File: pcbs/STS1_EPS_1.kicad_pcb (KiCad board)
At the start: 4 copper layers, 81 x 85 mm, 104 parts, among them J2 Panel X+, J3 Battery Pack, J4 Panel X-, J5 Panel Y+, J6 Panel Y-, J7 Panel Z+, Q1 SI7135DP-T1-GE3, U1 LTC4020EUHFPBF, U10 MAX11632EEGT, U11 TMCS1101A3B-Q1, U12 BD50GA5WEFJ, U13 TMCS1101A3B-Q1, U14 LM334M, U15 LM334M, U16 LM334M, U17 LM334M, U18 LM334M, U19 TMCS1101A3B-Q1, U20 TMCS1101A3B-Q1, U21 TMCS1101A3B-Q1, U22 TMCS1101A3B-Q1, U23 TMCS1101A3B-Q1, U24 TMCS1101A3B-Q1, U25 TMCS1101A3B-Q1, U26 TMCS1101A3B-Q1, U4 BQ29209DRBT, U5 MAX11632EEGT, U6 MAX11632EEGT, U7 MAX11632EEGT, U8 MAX11632EEGT, U9 MAX11632EEGT

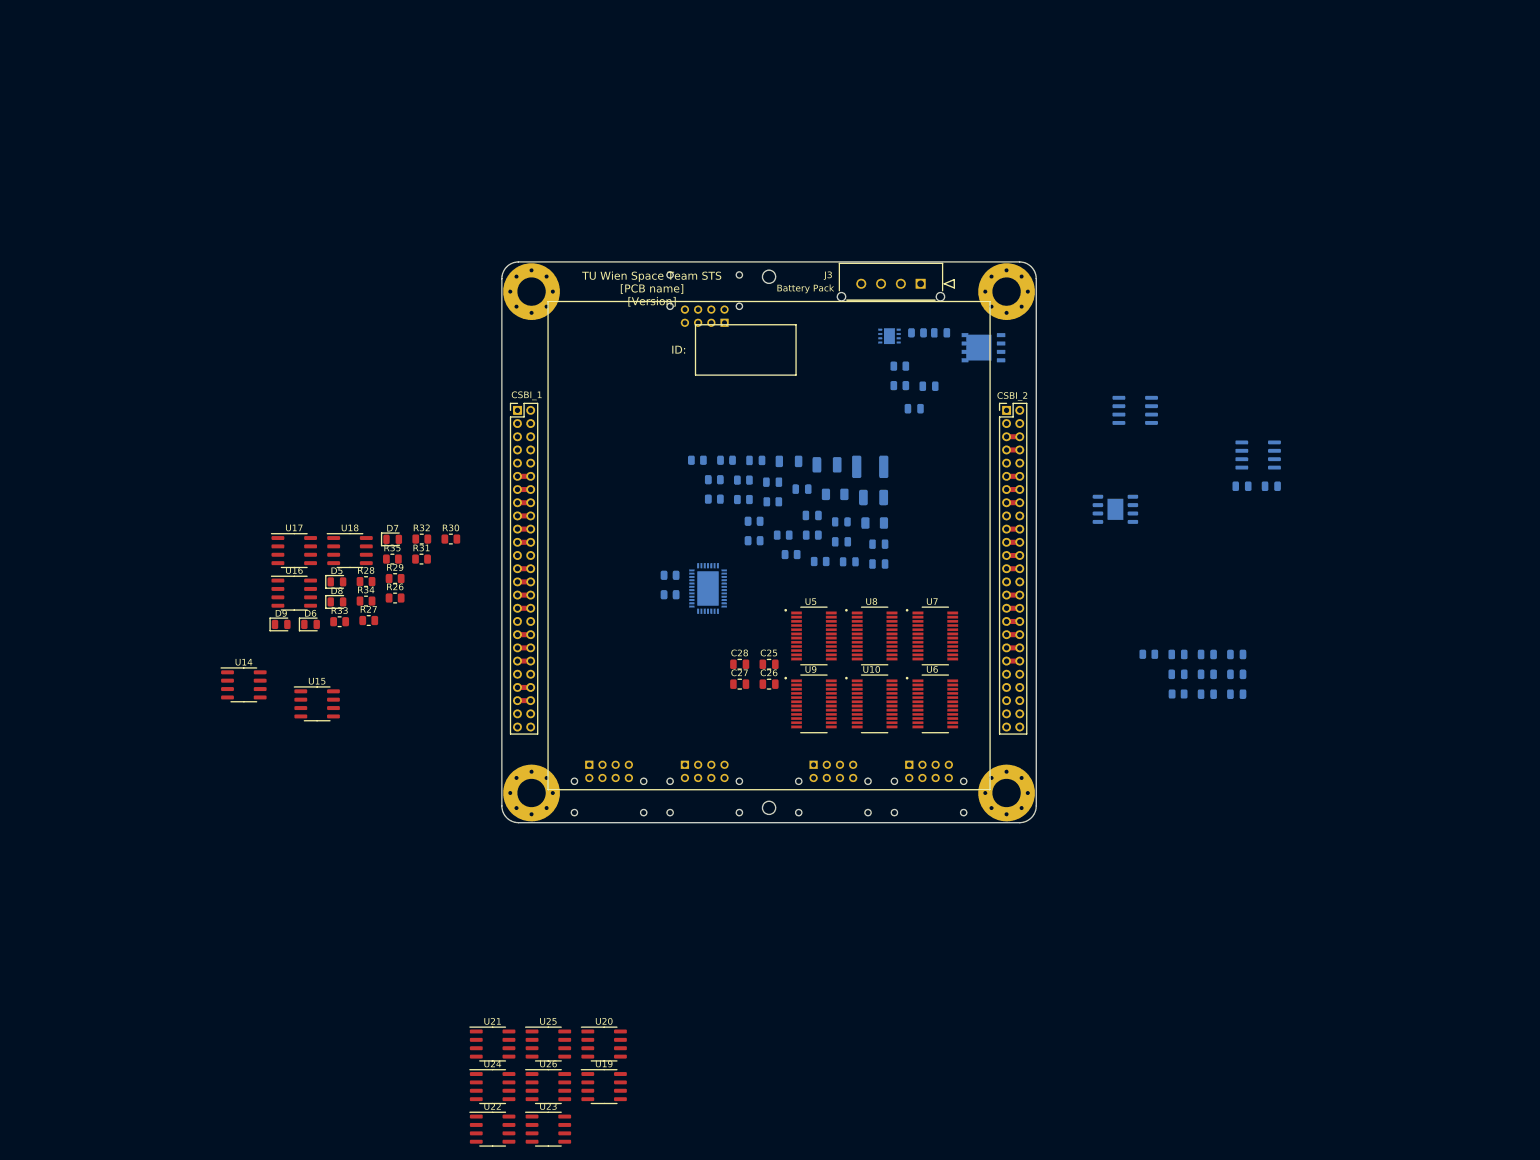
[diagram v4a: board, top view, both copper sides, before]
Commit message: Worked on STS_EPS_1.
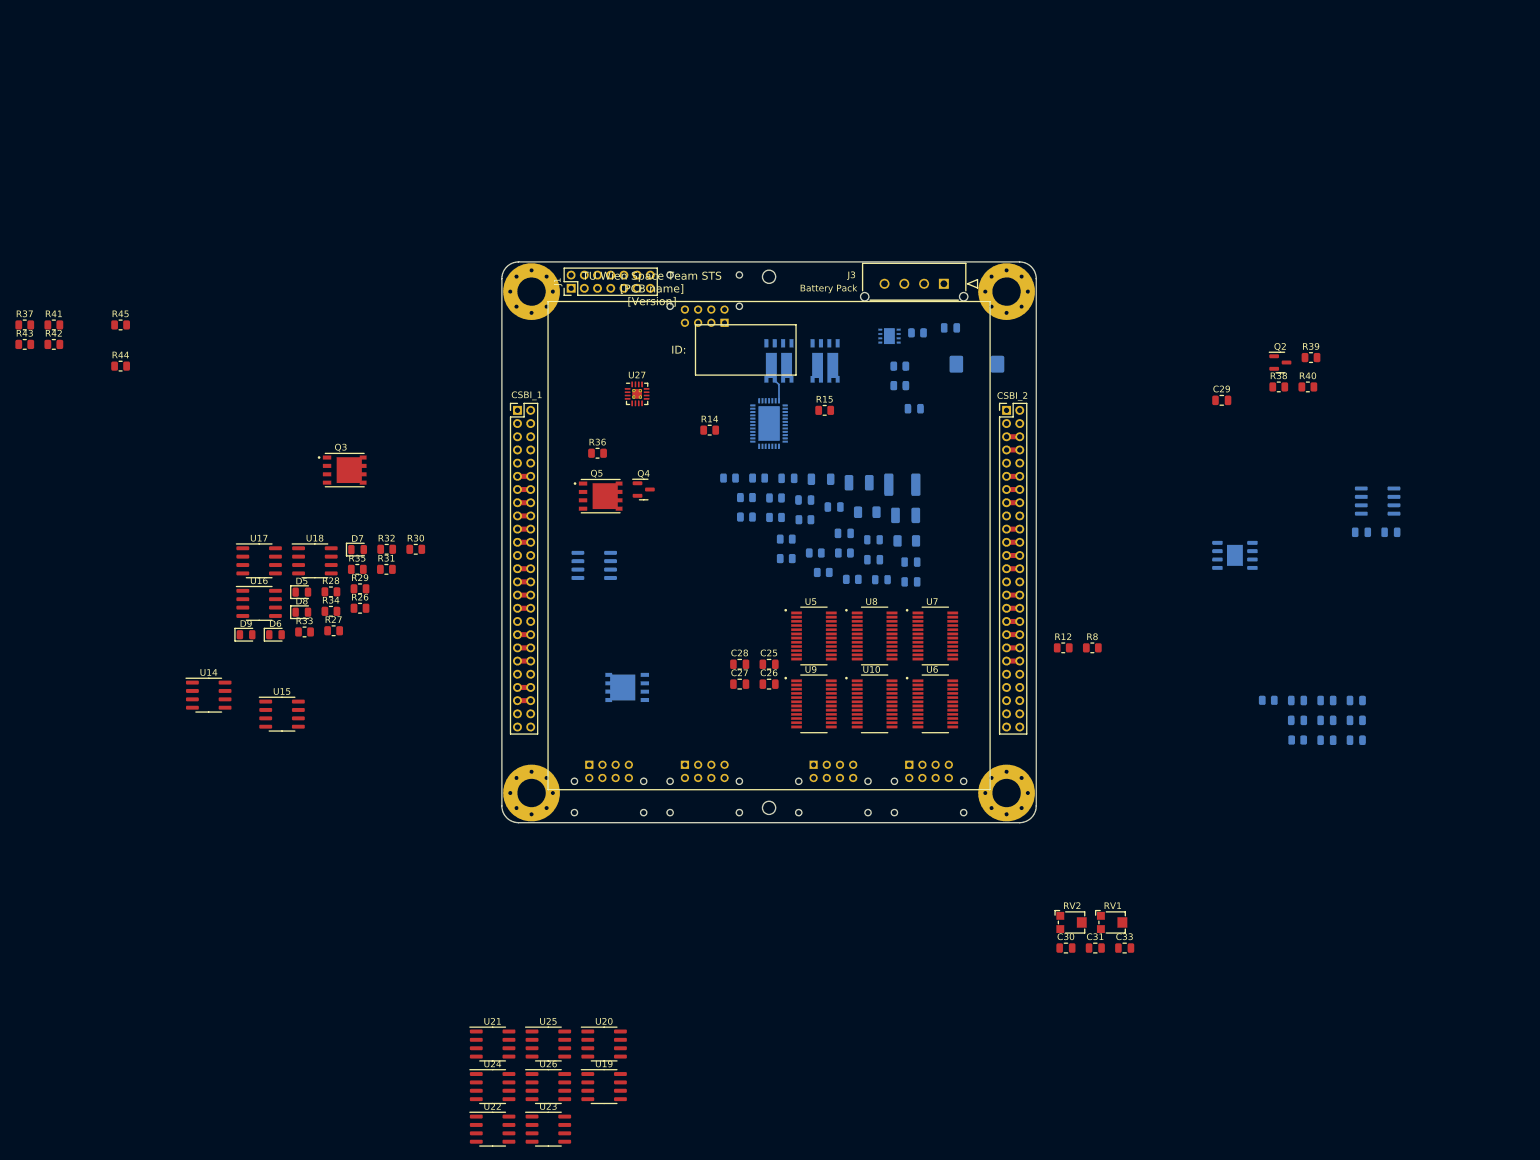
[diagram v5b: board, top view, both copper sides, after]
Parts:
- removed the C13 at (182.6, 52.5)
- removed the C13 at (180.9, 60.6)
- removed R16, R17: R, Resistor_SMD:R_0805_2012Metric
- added C13: 100n, Capacitor_SMD:C_0805_2012Metric, B.Cu at (184.1, 51.8)
- added C14: 330u, Capacitor_Tantalum_SMD:CP_EIA-7343-43_Kemet-X, B.Cu at (188.1, 57.3)
- added C29: 1u, Capacitor_SMD:C_0805_2012Metric, F.Cu at (225.3, 62.8)
- added C30: 10u, Capacitor_SMD:C_0805_2012Metric, F.Cu at (201.6, 145.8)
- added C31: 10u, Capacitor_SMD:C_0805_2012Metric, F.Cu at (206.1, 145.8)
- added C33: 100p, Capacitor_SMD:C_0805_2012Metric, F.Cu at (210.5, 145.8)
- added J1: Inter-EPS, Connector_PinHeader_2.00mm:PinHeader_2x07_P2.00mm_Vertical, F.Cu at (126.6, 45.8)
- added Q2: 2N7002, Package_TO_SOT_SMD:SOT-23, F.Cu at (234.1, 57.0)
- added Q3: SI7135DP-T1-GE3, STS_Package_SO:POWERPAK_SO8_single, F.Cu at (92.3, 73.4)
- added Q4: 2N7002, Package_TO_SOT_SMD:SOT-23, F.Cu at (137.6, 76.3)
- added Q5: SI7135DP-T1-GE3, STS_Package_SO:POWERPAK_SO8_single, F.Cu at (131.1, 77.3)
- added R12: 100k, Resistor_SMD:R_0805_2012Metric, F.Cu at (201.2, 100.3)
- added R14: 30m, Resistor_SMD:R_0805_2012Metric, F.Cu at (147.6, 67.3)
- added R15: 30m, Resistor_SMD:R_0805_2012Metric, F.Cu at (165.1, 64.3)
- added R36: R, Resistor_SMD:R_0805_2012Metric, F.Cu at (130.6, 70.8)
- added R37: 100k, Resistor_SMD:R_0805_2012Metric, F.Cu at (43.8, 51.4)
- added R38: 40k2, Resistor_SMD:R_0805_2012Metric, F.Cu at (233.9, 60.8)
- added R39: 64k, Resistor_SMD:R_0805_2012Metric, F.Cu at (238.8, 56.3)
- added R40: 31k5, Resistor_SMD:R_0805_2012Metric, F.Cu at (238.3, 60.8)
- added R41: 100k, Resistor_SMD:R_0805_2012Metric, F.Cu at (48.2, 51.4)
- added R42: 0, Resistor_SMD:R_0805_2012Metric, F.Cu at (48.2, 54.3)
- added R43: 0, Resistor_SMD:R_0805_2012Metric, F.Cu at (43.8, 54.3)
- added R44: 0, Resistor_SMD:R_0805_2012Metric, F.Cu at (58.3, 57.6)
- added R45: 0, Resistor_SMD:R_0805_2012Metric, F.Cu at (58.3, 51.4)
- added R8: 100k, Resistor_SMD:R_0805_2012Metric, F.Cu at (205.6, 100.3)
- added RV1: 50k, Potentiometer_SMD:Potentiometer_Bourns_TC33X_Vertical, F.Cu at (208.7, 141.9)
- added RV2: 50k, Potentiometer_SMD:Potentiometer_Bourns_TC33X_Vertical, F.Cu at (202.6, 141.9)
- added U2: SI7272DP-T1-GE3, STS_Package_SO:POWERPAK_SO8, B.Cu at (165.1, 53.7)
- added U27: TPS2420RSAT, Package_DFN_QFN:VQFN-16-1EP_3x3mm_P0.5mm_EP1.45x1.45mm_ThermalVias, F.Cu at (136.6, 61.8)
- added U3: SI7272DP-T1-GE3, STS_Package_SO:POWERPAK_SO8, B.Cu at (158.1, 53.7)
- C1, C5: value 220µ -> 50u
- CSBI_1, CSBI_2: value Conn_02x25_Odd_Even -> ~
- R1: value 17k8 -> 135k
- R13: value 200k -> 53k6
- R20: value 10m -> 17m
- R3: value 28k -> 180k
- R5: value 31k -> 155k
- R9: value 200k -> 166k
- moved U13 85.3 mm to (130.1, 87.8)
- moved Q1 74.6 mm to (135.1, 106.3)
- moved U1 26.7 mm to (156.6, 66.3)
- moved R25 19.4 mm to (236.8, 114.3)
- moved C15 19.4 mm to (250.9, 82.8)
- moved C16 19.4 mm to (246.4, 82.8)
- moved C17 19.4 mm to (236.7, 108.3)
- moved C18 19.4 mm to (241.2, 108.3)
- moved C19 19.4 mm to (241.2, 111.3)
- moved C20 19.4 mm to (245.6, 108.3)
- moved C21 19.4 mm to (245.6, 111.3)
- moved C22 19.4 mm to (241.2, 114.3)
- moved C23 19.4 mm to (236.7, 111.3)
- moved C24 19.4 mm to (245.6, 114.3)
- moved R24 19.4 mm to (232.3, 108.2)
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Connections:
- net /STS1_connector/EPS_BAT_GOOD renamed /BAT_GOOD
- net /STS1_connector/UART_COBC_EDU_1 renamed /Cubesat Bus Interface/UART_COBC_EDU_1
- net /STS1_connector/UART_COBC_EDU_2 renamed /Cubesat Bus Interface/UART_COBC_EDU_2
- net /STS1_connector/UCI_COBC_UART_1 renamed /Cubesat Bus Interface/UCI_COBC_UART_1
- net /STS1_connector/UCI_COBC_UART_2 renamed /Cubesat Bus Interface/UCI_COBC_UART_2
- net /Solar Cell Connectors/Panel_Y+_6 renamed /Panel_Y+_6
- net /Solar Cell Connectors/Panel_Y+_7 renamed /Panel_Y+_7
- net /Solar Cell Connectors/Panel_Y+_8 renamed /Panel_Y+_8
- net /Solar Cell Connectors/Panel_Y-_6 renamed /Panel_Y-_6
- net /Solar Cell Connectors/Panel_Y-_7 renamed /Panel_Y-_7
- net /Solar Cell Connectors/Panel_Y-_8 renamed /Panel_Y-_8
- net VBUS renamed /Bus Gate/VOUT_GATED
- C16 pad 1: /5V -> /+5V
- C8 pad 2: Net-(C8-Pad2) -> /Battery Charge Controller/SENSBOT
- CSBI_1 pad 11: /STS1_connector/EDU_SPI_6 -> /Analog Digital Converters/EDU_SPI_6
- CSBI_1 pad 12: /STS1_connector/EDU_SPI_6 -> /Analog Digital Converters/EDU_SPI_6
- CSBI_1 pad 13: /STS1_connector/EDU_SPI_5 -> /Analog Digital Converters/EDU_SPI_5
- CSBI_1 pad 14: /STS1_connector/EDU_SPI_5 -> /Analog Digital Converters/EDU_SPI_5
- CSBI_1 pad 15: /STS1_connector/EDU_SPI_4 -> /Analog Digital Converters/EDU_SPI_4
- CSBI_1 pad 16: /STS1_connector/EDU_SPI_4 -> /Analog Digital Converters/EDU_SPI_4
- CSBI_1 pad 17: /STS1_connector/EDU_SPI_3 -> /Analog Digital Converters/EDU_SPI_3
- CSBI_1 pad 18: /STS1_connector/EDU_SPI_3 -> /Analog Digital Converters/EDU_SPI_3
- CSBI_1 pad 19: /STS1_connector/EDU_SPI_2 -> /Analog Digital Converters/EDU_SPI_2
- CSBI_1 pad 20: /STS1_connector/EDU_SPI_2 -> /Analog Digital Converters/EDU_SPI_2
- CSBI_1 pad 21: /STS1_connector/EDU_SPI_1 -> /Analog Digital Converters/EDU_SPI_1
- CSBI_1 pad 22: /STS1_connector/EDU_SPI_1 -> /Analog Digital Converters/EDU_SPI_1
- CSBI_1 pad 25: Net-(CSBI_1-Pad25) -> unconnected-(CSBI_1-Pad25)
- CSBI_1 pad 26: Net-(CSBI_1-Pad25) -> unconnected-(CSBI_1-Pad25)
- CSBI_1 pad 27: Net-(CSBI_1-Pad27) -> unconnected-(CSBI_1-Pad27)
- CSBI_1 pad 28: Net-(CSBI_1-Pad27) -> unconnected-(CSBI_1-Pad27)
- CSBI_1 pad 29: Net-(CSBI_1-Pad29) -> unconnected-(CSBI_1-Pad29)
- CSBI_1 pad 30: Net-(CSBI_1-Pad29) -> unconnected-(CSBI_1-Pad29)
- CSBI_1 pad 31: Net-(CSBI_1-Pad31) -> unconnected-(CSBI_1-Pad31)
- CSBI_1 pad 32: Net-(CSBI_1-Pad31) -> unconnected-(CSBI_1-Pad31)
- CSBI_1 pad 35: /STS1_connector/EDU_Heartbeat -> unconnected-(CSBI_1-Pad35)
- CSBI_1 pad 36: /STS1_connector/EDU_Heartbeat -> unconnected-(CSBI_1-Pad35)
- CSBI_1 pad 37: /STS1_connector/EDU_UPDATE -> unconnected-(CSBI_1-Pad37)
- CSBI_1 pad 38: /STS1_connector/EDU_UPDATE -> unconnected-(CSBI_1-Pad37)
- CSBI_1 pad 39: /STS1_connector/EDU_EN -> unconnected-(CSBI_1-Pad39)
- CSBI_1 pad 40: /STS1_connector/EDU_EN -> unconnected-(CSBI_1-Pad39)
- CSBI_2 pad 11: Net-(CSBI_2-Pad11) -> unconnected-(CSBI_2-Pad11)
- CSBI_2 pad 12: Net-(CSBI_2-Pad11) -> unconnected-(CSBI_2-Pad11)
- CSBI_2 pad 13: Net-(CSBI_2-Pad13) -> /BAT_FAULT
- CSBI_2 pad 14: Net-(CSBI_2-Pad13) -> /BAT_FAULT
- CSBI_2 pad 15: /STS1_connector/EDU_BOOT -> unconnected-(CSBI_2-Pad15)
- CSBI_2 pad 16: /STS1_connector/EDU_BOOT -> unconnected-(CSBI_2-Pad15)
- CSBI_2 pad 19: /STS1_connector/UCI_COBC_3V3 -> unconnected-(CSBI_2-Pad19)
- CSBI_2 pad 20: /STS1_connector/UCI_COBC_3V3 -> unconnected-(CSBI_2-Pad20)
- CSBI_2 pad 23: /STS1_connector/EPS_ANT_DEPLOYED -> unconnected-(CSBI_2-Pad23)
- CSBI_2 pad 24: /STS1_connector/EPS_ANT_DEPLOYED -> unconnected-(CSBI_2-Pad24)
- CSBI_2 pad 25: /STS1_connector/EPS_CHARGING -> /BAT_CHARGING
- CSBI_2 pad 26: /STS1_connector/EPS_CHARGING -> /BAT_CHARGING
- CSBI_2 pad 29: /STS1_connector/COBC_SPI_1 -> /Analog Digital Converters/COBC_SPI_1
- CSBI_2 pad 30: /STS1_connector/COBC_SPI_1 -> /Analog Digital Converters/COBC_SPI_1
- CSBI_2 pad 31: /STS1_connector/COBC_SPI_2 -> /Analog Digital Converters/COBC_SPI_2
- CSBI_2 pad 32: /STS1_connector/COBC_SPI_2 -> /Analog Digital Converters/COBC_SPI_2
- CSBI_2 pad 33: /STS1_connector/COBC_SPI_3 -> /Analog Digital Converters/COBC_SPI_3
- CSBI_2 pad 34: /STS1_connector/COBC_SPI_3 -> /Analog Digital Converters/COBC_SPI_3
- CSBI_2 pad 35: /STS1_connector/COBC_SPI_4 -> /Analog Digital Converters/COBC_SPI_4
- CSBI_2 pad 36: /STS1_connector/COBC_SPI_4 -> /Analog Digital Converters/COBC_SPI_4
- CSBI_2 pad 37: /STS1_connector/COBC_SPI_5 -> /Analog Digital Converters/COBC_SPI_5
- CSBI_2 pad 38: /STS1_connector/COBC_SPI_5 -> /Analog Digital Converters/COBC_SPI_5
- CSBI_2 pad 39: /STS1_connector/COBC_SPI_6 -> /Analog Digital Converters/COBC_SPI_6
- CSBI_2 pad 40: /STS1_connector/COBC_SPI_6 -> /Analog Digital Converters/COBC_SPI_6
- J2 pad 1: /Solar Cell Connectors/Panel_X+_1 -> /Panel_X+_1
- J2 pad 2: /Solar Cell Connectors/Panel_X+_2 -> /Panel_X+_2
- J2 pad 3: /Solar Cell Connectors/Panel_X+_3 -> /Panel_X+_3
- J2 pad 5: /Solar Cell Connectors/Panel_X+_5 -> /Panel_X+_5
- J2 pad 6: /Solar Cell Connectors/Panel_X+_6 -> /Panel_X+_6
- J2 pad 7: /Solar Cell Connectors/Panel_X+_7 -> /Panel_X+_7
- J2 pad 8: /Solar Cell Connectors/Panel_X+_8 -> /Panel_X+_8
- J3 pad 2: GND -> GNDREF
- J4 pad 1: /Solar Cell Connectors/Panel_X-_1 -> /Panel_X-_1
- J4 pad 2: /Solar Cell Connectors/Panel_X-_2 -> /Panel_X-_2
- J4 pad 3: /Solar Cell Connectors/Panel_X-_3 -> /Panel_X-_3
- J4 pad 5: /Solar Cell Connectors/Panel_X-_5 -> /Panel_X-_5
- J4 pad 6: /Solar Cell Connectors/Panel_X-_6 -> /Panel_X-_6
- J4 pad 7: /Solar Cell Connectors/Panel_X-_7 -> /Panel_X-_7
- J4 pad 8: /Solar Cell Connectors/Panel_X-_8 -> /Panel_X-_8
- J5 pad 1: /Solar Cell Connectors/Panel_Y+_1 -> /Panel_Y+_1
- J5 pad 2: /Solar Cell Connectors/Panel_Y+_2 -> /Panel_Y+_2
- J5 pad 3: /Solar Cell Connectors/Panel_Y+_3 -> /Panel_Y+_3
- J5 pad 5: /Solar Cell Connectors/Panel_Y+_5 -> /Panel_Y+_5
- J6 pad 1: /Solar Cell Connectors/Panel_Y-_1 -> /Panel_Y-_1
- J6 pad 2: /Solar Cell Connectors/Panel_Y-_2 -> /Panel_Y-_2
- J6 pad 3: /Solar Cell Connectors/Panel_Y-_3 -> /Panel_Y-_3
- J6 pad 5: /Solar Cell Connectors/Panel_Y-_5 -> /Panel_Y-_5
- J7 pad 1: /Solar Cell Connectors/Panel_Z+_1 -> /Panel_Z+_1
- J7 pad 2: /Solar Cell Connectors/Panel_Z+_2 -> /Panel_Z+_2
- J7 pad 3: /Solar Cell Connectors/Panel_Z+_3 -> /Panel_Z+_3
- J7 pad 5: /Solar Cell Connectors/Panel_Z+_5 -> /Panel_Z+_5
- J7 pad 6: /Solar Cell Connectors/Panel_Z+_6 -> /Panel_Z+_6
- J7 pad 7: /Solar Cell Connectors/Panel_Z+_7 -> /Panel_Z+_7
- J7 pad 8: /Solar Cell Connectors/Panel_Z+_8 -> /Panel_Z+_8
- Q1 pad 2: (no net) -> Net-(Q1-Pad1)
- Q1 pad 3: (no net) -> Net-(Q1-Pad1)
- U1 pad 12: /Battery Charge Controller/STAT1 -> /BAT_CHARGING
- U1 pad 36: /MPPT_BUS -> /DS1_L
- U1 pad 7: /Battery Charge Controller/SENSVIN -> /DS1_L
- U11 pad 1: unconnected-(U11-Pad1) -> /MPPT Bus Junction/MPPT_SUM
- U11 pad 2: unconnected-(U11-Pad2) -> /MPPT Bus Junction/MPPT_SUM
- U11 pad 3: /MPPT_BUS -> /DS1_H
- U11 pad 4: unconnected-(U11-Pad4) -> /DS1_H
- U11 pad 7: /MPPT_I -> /MPPT_I_SUM
- U12 pad 1: /5V -> /+5V
- U12 pad 2: /5V -> /+5V
- U13 pad 1: /Battery/Battery Inhibits/BATT_INHIBIT -> /Battery Charge Controller/BATT
- U13 pad 2: /Battery/Battery Inhibits/BATT_INHIBIT -> /Battery Charge Controller/BATT
- U19 pad 1: /MPPT Current Sensors/MPPT_X+_1_IN -> /Panel_X+_3
- U19 pad 2: /MPPT Current Sensors/MPPT_X+_1_IN -> /Panel_X+_3
- U19 pad 3: /MPPT Current Sensors/MPPT_X+_1_OUT -> /MPPT Bus Junction/MPPT_SUM
- U19 pad 4: /MPPT Current Sensors/MPPT_X+_1_OUT -> /MPPT Bus Junction/MPPT_SUM
- U19 pad 5: /MPPT Current Sensors/5V -> /5V
- U19 pad 7: /MPPT Current Sensors/MPPT_X+_1_I -> /MPPT_X+_1_I
- U20 pad 1: /MPPT Current Sensors/MPPT_X+_2_IN -> /Panel_X+_6
- U20 pad 2: /MPPT Current Sensors/MPPT_X+_2_IN -> /Panel_X+_6
- U20 pad 3: /MPPT Current Sensors/MPPT_X+_2_OUT -> /MPPT Bus Junction/MPPT_SUM
- U20 pad 4: /MPPT Current Sensors/MPPT_X+_2_OUT -> /MPPT Bus Junction/MPPT_SUM
- U20 pad 5: /MPPT Current Sensors/5V -> /5V
- U20 pad 7: /MPPT Current Sensors/MPPT_X+_2_I -> /MPPT_X+_2_I
- U21 pad 1: /MPPT Current Sensors/MPPT_X-_1_IN -> /Panel_X-_3
- U21 pad 2: /MPPT Current Sensors/MPPT_X-_1_IN -> /Panel_X-_3
- U21 pad 3: /MPPT Current Sensors/MPPT_X-_1_OUT -> /MPPT Bus Junction/MPPT_SUM
- U21 pad 4: /MPPT Current Sensors/MPPT_X-_1_OUT -> /MPPT Bus Junction/MPPT_SUM
- U21 pad 5: /MPPT Current Sensors/5V -> /5V
- U21 pad 7: /MPPT Current Sensors/MPPT_X-_1_I -> /MPPT_X-_1_I
- U22 pad 1: /MPPT Current Sensors/MPPT_X-_2_IN -> /Panel_X-_6
- U22 pad 2: /MPPT Current Sensors/MPPT_X-_2_IN -> /Panel_X-_6
- U22 pad 3: /MPPT Current Sensors/MPPT_X-_2_OUT -> /MPPT Bus Junction/MPPT_SUM
- U22 pad 4: /MPPT Current Sensors/MPPT_X-_2_OUT -> /MPPT Bus Junction/MPPT_SUM
- U22 pad 5: /MPPT Current Sensors/5V -> /5V
- U22 pad 7: /MPPT Current Sensors/MPPT_X-_2_I -> /MPPT_X-_2_I
- U23 pad 1: /MPPT Current Sensors/MPPT_Y+_1_IN -> /Panel_Y+_3
- U23 pad 2: /MPPT Current Sensors/MPPT_Y+_1_IN -> /Panel_Y+_3
- U23 pad 3: /MPPT Current Sensors/MPPT_Y+_1_OUT -> /MPPT Bus Junction/MPPT_SUM
- U23 pad 4: /MPPT Current Sensors/MPPT_Y+_1_OUT -> /MPPT Bus Junction/MPPT_SUM
- U23 pad 5: /MPPT Current Sensors/5V -> /5V
- U23 pad 7: /MPPT Current Sensors/MPPT_Y+_1_I -> /MPPT_Y+_1_I
- U24 pad 1: /MPPT Current Sensors/MPPT_Y-_1_IN -> /Panel_Y-_3
- U24 pad 2: /MPPT Current Sensors/MPPT_Y-_1_IN -> /Panel_Y-_3
- U24 pad 3: /MPPT Current Sensors/MPPT_Y-_1_OUT -> /MPPT Bus Junction/MPPT_SUM
- U24 pad 4: /MPPT Current Sensors/MPPT_Y-_1_OUT -> /MPPT Bus Junction/MPPT_SUM
- U24 pad 5: /MPPT Current Sensors/5V -> /5V
- U24 pad 7: /MPPT Current Sensors/MPPT_Y-_1_I -> /MPPT_Y-_1_I
- U25 pad 1: /MPPT Current Sensors/MPPT_Z+_1_IN -> /Panel_Z+_3
- U25 pad 2: /MPPT Current Sensors/MPPT_Z+_1_IN -> /Panel_Z+_3
- U25 pad 3: /MPPT Current Sensors/MPPT_Z+_1_OUT -> /MPPT Bus Junction/MPPT_SUM
- U25 pad 4: /MPPT Current Sensors/MPPT_Z+_1_OUT -> /MPPT Bus Junction/MPPT_SUM
- U25 pad 5: /MPPT Current Sensors/5V -> /5V
- U25 pad 7: /MPPT Current Sensors/MPPT_Z+_1_I -> /MPPT_Z+_1_I
- U26 pad 1: /MPPT Current Sensors/MPPT_Z+_2_IN -> /Panel_Z+_6
- U26 pad 2: /MPPT Current Sensors/MPPT_Z+_2_IN -> /Panel_Z+_6
- U26 pad 3: /MPPT Current Sensors/MPPT_Z+_2_OUT -> /MPPT Bus Junction/MPPT_SUM
- U26 pad 4: /MPPT Current Sensors/MPPT_Z+_2_OUT -> /MPPT Bus Junction/MPPT_SUM
- U26 pad 5: /MPPT Current Sensors/5V -> /5V
- U26 pad 7: /MPPT Current Sensors/MPPT_Z+_2_I -> /MPPT_X+_2_I
- U4 pad 5: GND -> GNDREF
- U4 pad 9: GND -> GNDREF
- U6 pad 10: GND -> /VOUT_I
- U7 pad 1: /Analog Digital Converters/MPPT_I_SUM -> /MPPT_I_SUM
- U7 pad 10: /MPPT_BUS -> /DS1_L
- U7 pad 11: unconnected-(U7-Pad11) -> GND
- U7 pad 12: unconnected-(U7-Pad12) -> GND
- U7 pad 13: unconnected-(U7-Pad13) -> GND
- U7 pad 14: unconnected-(U7-Pad14) -> GND
- U7 pad 15: unconnected-(U7-Pad15) -> GND
- U7 pad 16: unconnected-(U7-Pad16) -> GND
- U7 pad 2: /Analog Digital Converters/MPPT_I_X+_1 -> /MPPT_X+_1_I
- U7 pad 3: /Analog Digital Converters/MPPT_I_X+_2 -> /MPPT_X+_2_I
- U7 pad 4: /Analog Digital Converters/MPPT_I_X-_1 -> /MPPT_X-_1_I
- U7 pad 5: /Analog Digital Converters/MPPT_I_X-_2 -> /MPPT_X-_2_I
- U7 pad 6: /Analog Digital Converters/MPPT_I_Y+_1 -> /MPPT_Y+_1_I
- U7 pad 7: /Analog Digital Converters/MPPT_I_Y-_1 -> /MPPT_Y-_1_I
- U7 pad 8: /MPPT_I_Z+_1 -> /MPPT_Z+_1_I
- U7 pad 9: /Analog Digital Converters/MPPT_I_Z+_2 -> /MPPT_X+_2_I
- U8 pad 10: GND -> /VOUT_I
- U9 pad 1: /Analog Digital Converters/MPPT_I_SUM -> /MPPT_I_SUM
- U9 pad 10: /MPPT_BUS -> /DS1_L
- U9 pad 11: unconnected-(U9-Pad11) -> GND
- U9 pad 12: unconnected-(U9-Pad12) -> GND
- U9 pad 13: unconnected-(U9-Pad13) -> GND
- U9 pad 14: unconnected-(U9-Pad14) -> GND
- U9 pad 15: unconnected-(U9-Pad15) -> GND
- U9 pad 16: unconnected-(U9-Pad16) -> GND
- U9 pad 2: /Analog Digital Converters/MPPT_I_X+_1 -> /MPPT_X+_1_I
- U9 pad 3: /Analog Digital Converters/MPPT_I_X+_2 -> /MPPT_X+_2_I
- U9 pad 4: /Analog Digital Converters/MPPT_I_X-_1 -> /MPPT_X-_1_I
- U9 pad 5: /Analog Digital Converters/MPPT_I_X-_2 -> /MPPT_X-_2_I
- U9 pad 6: /Analog Digital Converters/MPPT_I_Y+_1 -> /MPPT_Y+_1_I
- U9 pad 7: /Analog Digital Converters/MPPT_I_Y-_1 -> /MPPT_Y-_1_I
- U9 pad 8: /MPPT_I_Z+_1 -> /MPPT_Z+_1_I
- U9 pad 9: /Analog Digital Converters/MPPT_I_Z+_2 -> /MPPT_X+_2_I
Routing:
- net /Battery Charge Controller/SW1: track 0.00 -> 3.36 mm
- net unconnected-(CSBI_2-Pad23): track 0.00 -> 2.00 mm
- net unconnected-(CSBI_2-Pad19): track 0.00 -> 2.00 mm
- net unconnected-(CSBI_2-Pad15): track 0.00 -> 2.00 mm
- net unconnected-(CSBI_2-Pad11): track 0.00 -> 2.00 mm
- net unconnected-(CSBI_1-Pad39): track 0.00 -> 2.00 mm
- net unconnected-(CSBI_1-Pad37): track 0.00 -> 2.00 mm
- net unconnected-(CSBI_1-Pad35): track 0.00 -> 2.00 mm
- net unconnected-(CSBI_1-Pad31): track 0.00 -> 2.00 mm
- net unconnected-(CSBI_1-Pad29): track 0.00 -> 2.00 mm
- net unconnected-(CSBI_1-Pad27): track 0.00 -> 2.00 mm
- net unconnected-(CSBI_1-Pad25): track 0.00 -> 2.00 mm
- net Net-(CSBI_2-Pad13): track 2.00 -> 0.00 mm
- net Net-(CSBI_2-Pad11): track 2.00 -> 0.00 mm
- net Net-(CSBI_1-Pad31): track 2.00 -> 0.00 mm
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
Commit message: Worked on STS1_EPS_1 and began work on STS1_EPS_2.
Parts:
- added C32: 680u, Capacitor_Tantalum_SMD:CP_EIA-7343-43_Kemet-X, F.Cu at (143.8, 19.3)
- added C34: 100n, Capacitor_SMD:C_0805_2012Metric, F.Cu at (172.6, 34.1)
- added C35: 100n, Capacitor_SMD:C_0805_2012Metric, F.Cu at (177.1, 34.1)
- added C4: 680u, Capacitor_Tantalum_SMD:CP_EIA-7343-43_Kemet-X, F.Cu at (131.6, 19.5)
- added L1: 100u, Inductor_SMD:L_Vishay_IHLP-4040, F.Cu at (216.8, 34.5)
- added U28: LTC4451AV#TRMPBF, STS_Package_DFN_QFN:AD_LQFN-16, F.Cu at (185.4, 74.1)
- added U29: LTC4451AV#TRMPBF, STS_Package_DFN_QFN:AD_LQFN-16, F.Cu at (171.8, 66.1)
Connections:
- U27 pad 1: /DS4_L -> Net-(U27-Pad1)
- U27 pad 2: /DS4_L -> Net-(U27-Pad1)
- U27 pad 3: /DS4_L -> Net-(U27-Pad1)
- U27 pad 4: /DS4_L -> Net-(U27-Pad1)

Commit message: Finished first revision of schematic.
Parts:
- removed C29: 1u, Capacitor_SMD:C_0805_2012Metric
- removed C34, C35: 100n, Capacitor_SMD:C_0805_2012Metric
- removed Q2, Q4: 2N7002, Package_TO_SOT_SMD:SOT-23
- removed Q3, Q5: SI7135DP-T1-GE3, STS_Package_SO:POWERPAK_SO8_single
- removed R37, R41: 100k, Resistor_SMD:R_0805_2012Metric
- removed R38: 40k2, Resistor_SMD:R_0805_2012Metric
- removed R39: 64k, Resistor_SMD:R_0805_2012Metric
- removed R40: 31k5, Resistor_SMD:R_0805_2012Metric
- removed R42, R43: 0, Resistor_SMD:R_0805_2012Metric
- removed U27: TPS2420RSAT, Package_DFN_QFN:VQFN-16-1EP_3x3mm_P0.5mm_EP1.45x1.45mm_ThermalVias
- removed U28, U29: LTC4451AV#TRMPBF, STS_Package_DFN_QFN:AD_LQFN-16
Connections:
- net /Battery Charge Controller/VOUT renamed /BCC_OUT
- net /VOUT renamed /INTERNAL_V
- C19 pad 1: /5V -> /+5V
- C20 pad 1: /5V -> /+5V
- C21 pad 1: /5V -> /+5V
- C22 pad 1: /5V -> /+5V
- C23 pad 1: /5V -> /+5V
- C24 pad 1: /5V -> /+5V
- CSBI_1 pad 5: /Bus Gate/VOUT_GATED -> unconnected-(CSBI_1-Pad5)
- CSBI_1 pad 6: /Bus Gate/VOUT_GATED -> unconnected-(CSBI_1-Pad5)
- CSBI_1 pad 7: /Bus Gate/VOUT_GATED -> unconnected-(CSBI_1-Pad5)
- CSBI_1 pad 8: /Bus Gate/VOUT_GATED -> unconnected-(CSBI_1-Pad5)
- CSBI_2 pad 13: /BAT_FAULT -> unconnected-(CSBI_2-Pad13)
- CSBI_2 pad 14: /BAT_FAULT -> unconnected-(CSBI_2-Pad13)
- CSBI_2 pad 21: /BAT_GOOD -> unconnected-(CSBI_2-Pad21)
- CSBI_2 pad 22: /BAT_GOOD -> unconnected-(CSBI_2-Pad21)
- CSBI_2 pad 43: /Bus Gate/VOUT_GATED -> unconnected-(CSBI_2-Pad43)
- CSBI_2 pad 44: /Bus Gate/VOUT_GATED -> unconnected-(CSBI_2-Pad43)
- CSBI_2 pad 45: /Bus Gate/VOUT_GATED -> unconnected-(CSBI_2-Pad43)
- CSBI_2 pad 46: /Bus Gate/VOUT_GATED -> unconnected-(CSBI_2-Pad43)
- J1 pad 10: /DS3_H -> unconnected-(J1-Pad10)
- J1 pad 11: GND -> unconnected-(J1-Pad11)
- J1 pad 12: /DS4_L -> unconnected-(J1-Pad12)
- J1 pad 13: /DS3_H -> unconnected-(J1-Pad13)
- J1 pad 14: /DS4_L -> unconnected-(J1-Pad14)
- J1 pad 5: GNDREF -> unconnected-(J1-Pad5)
- J1 pad 6: /DT_SIGNAL -> unconnected-(J1-Pad6)
- J1 pad 7: GNDREF -> unconnected-(J1-Pad7)
- J1 pad 8: /RBF_SIGNAL -> unconnected-(J1-Pad8)
- J1 pad 9: GND -> unconnected-(J1-Pad9)
- U10 pad 19: /5V -> /+5V
- U11 pad 5: /5V -> /+5V
- U14 pad 4: /5V -> /+5V
- U15 pad 4: /5V -> /+5V
- U16 pad 4: /5V -> /+5V
- U17 pad 4: /5V -> /+5V
- U18 pad 4: /5V -> /+5V
- U19 pad 5: /5V -> /+5V
- U20 pad 5: /5V -> /+5V
- U21 pad 5: /5V -> /+5V
- U22 pad 5: /5V -> /+5V
- U23 pad 5: /5V -> /+5V
- U24 pad 5: /5V -> /+5V
- U25 pad 5: /5V -> /+5V
- U26 pad 5: /5V -> /+5V
- U5 pad 19: /5V -> /+5V
- U6 pad 19: /5V -> /+5V
- U7 pad 19: /5V -> /+5V
- U8 pad 19: /5V -> /+5V
- U9 pad 19: /5V -> /+5V
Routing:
- net unconnected-(CSBI_2-Pad24): track 0.00 -> 2.00 mm
- net unconnected-(CSBI_2-Pad23): track 2.00 -> 0.00 mm
- net unconnected-(CSBI_2-Pad21): track 0.00 -> 2.00 mm
- net unconnected-(CSBI_2-Pad13): track 0.00 -> 2.00 mm
- net /BAT_GOOD: track 2.00 -> 0.00 mm
- net /BAT_FAULT: track 2.00 -> 0.00 mm
